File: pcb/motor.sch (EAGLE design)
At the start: 8 parts, among them Q1 BC847, X1 X1

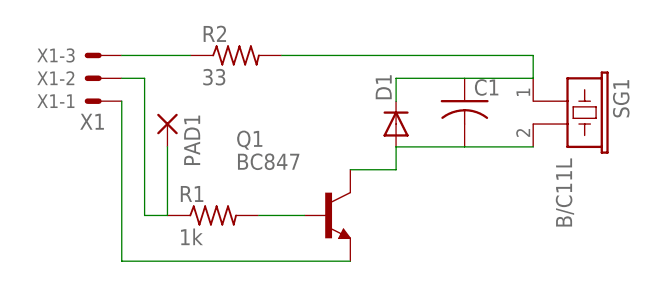
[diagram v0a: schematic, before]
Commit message: Added an extra pad for the control signal on motor board.
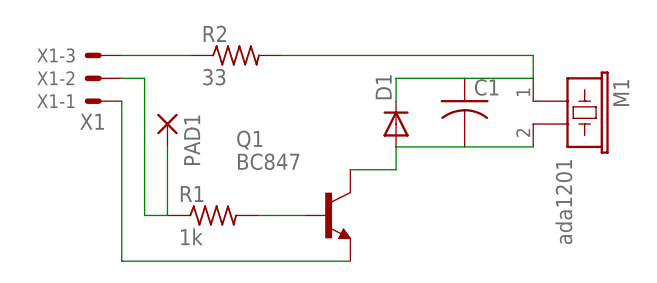
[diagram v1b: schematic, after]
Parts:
- M1: value B/C11L -> ada1201
- renumbered SG1 to M1
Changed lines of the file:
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@@
 <parts>
 <part name="Q1" library="transistor-npn" deviceset="BCX70*" device="SMD" value="BC847"/>
-<part name="SG1" library="buzzer" deviceset="B/C11L" device=""/>
+<part name="M1" library="buzzer" deviceset="B/C11L" device="" value="ada1201"/>
 <part name="R1" library="resistor" deviceset="R-US_" device="R0805" value="1k"/>
 <part name="R2" library="resistor" deviceset="R-US_" device="R0805" value="33"/>
@@
 <instances>
 <instance part="Q1" gate="G$1" x="25.4" y="30.48"/>
-<instance part="SG1" gate="G$1" x="50.8" y="43.18" rot="R270"/>
+<instance part="M1" gate="G$1" x="50.8" y="43.18" rot="R270"/>
 <instance part="R1" gate="G$1" x="12.7" y="30.48"/>
 <instance part="R2" gate="G$1" x="15.24" y="48.26"/>
@@
 <pinref part="C1" gate="G$1" pin="2"/>
 <wire x1="40.64" y1="38.1" x2="33.02" y2="38.1" width="0.1524" layer="91"/>
-<pinref part="SG1" gate="G$1" pin="2"/>
+<pinref part="M1" gate="G$1" pin="2"/>
 <wire x1="48.26" y1="38.1" x2="40.64" y2="38.1" width="0.1524" layer="91"/>
 </segment>
@@
 <pinref part="C1" gate="G$1" pin="1"/>
 <wire x1="33.02" y1="45.72" x2="40.64" y2="45.72" width="0.1524" layer="91"/>
-<pinref part="SG1" gate="G$1" pin="1"/>
+<pinref part="M1" gate="G$1" pin="1"/>
 <wire x1="48.26" y1="45.72" x2="40.64" y2="45.72" width="0.1524" layer="91"/>
 <pinref part="R2" gate="G$1" pin="2"/>
